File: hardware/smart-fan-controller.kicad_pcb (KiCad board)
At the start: 2 copper layers, 80 x 60 mm, 20 parts, among them J1 SATA-15PIN-PWR, J2 USB-C 16P, J3 FAN1, J4 FAN2, J5 FAN3, J6 FAN4, J7 DS18B20-1, J8 DS18B20-2, SW1 RST, SW2 BOOT, SW3 WIFI CFG, U1 AMS1117-3.3 SOT-223, U2 ESP32-S3-WROOM-1-N16R8, U3 74AHCT125 SOIC-14, U4 BME280 LGA-8

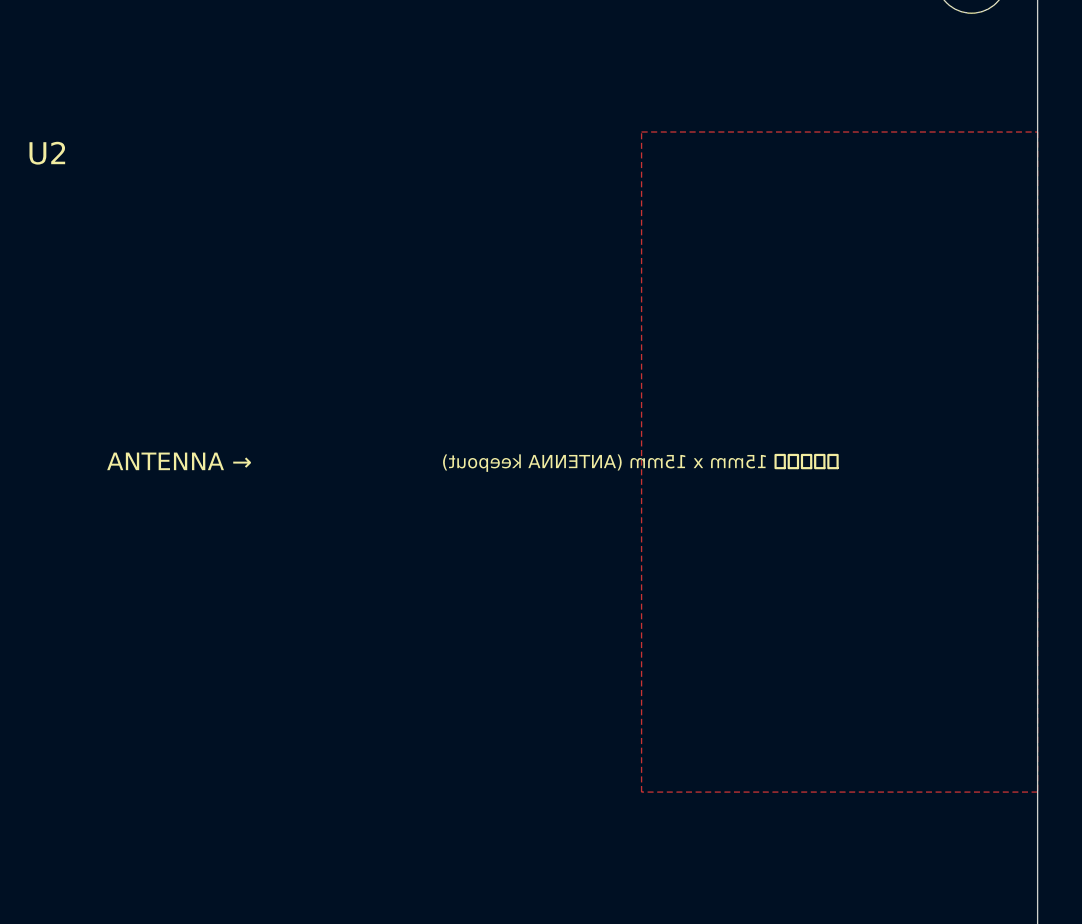
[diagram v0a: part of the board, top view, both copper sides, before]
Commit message: fix: remove v7 keepout zone for KiCad v10 compatibility
- KiCad v7 format (version 20221018) incompatible with v10
- Remove zone definition to allow file to open in v10
- Keepout area marked with silkscreen text for manual re-creation
- v10 will auto-upgrade file format on first save
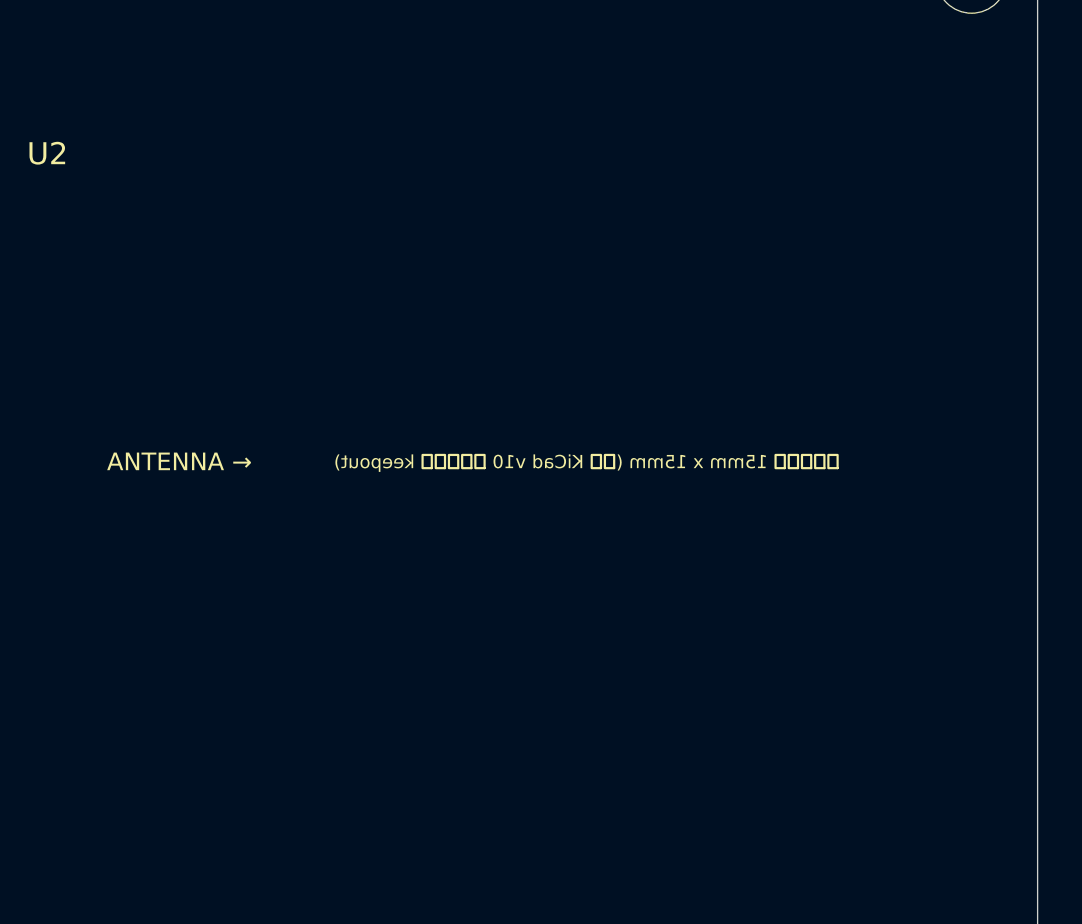
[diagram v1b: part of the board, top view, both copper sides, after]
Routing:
- removed copper zone on F.Cu, net 0
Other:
- board text added: "天线禁布区 15mm x 15mm (需在 KiCad v10 中手动添加 keepout)"
- board text removed: "天线禁布区 15mm x 15mm (ANTENNA keepout)"
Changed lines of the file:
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@@
     )
   )
-  (zone
-    (net 0) (net_name "")
-    (layer "F.Cu")
-    (name "ANTENNA_KEEPOUT_15mm")
-    (hatch edge 0.5)
-    (connect_pads (clearance 0))
-    (min_thickness 0.25)
-    (keepout_constraints
-      (kcq_tracks no) (kcq_vias no) (kcq_copperpour no)
-      (kcq_footprints no) (kcq_text no)
-    )
-    (polygon
-      (pts
-        (xy 62 10) (xy 80 10) (xy 80 40) (xy 62 40)
-      )
-    )
-  )
-  (gr_text "天线禁布区 15mm x 15mm (ANTENNA keepout)" (at 71 25 0)
+  (gr_text "天线禁布区 15mm x 15mm (需在 KiCad v10 中手动添加 keepout)" (at 71 25 0)
     (layer "F.SilkS")
     (effects (font (size 0.6 0.6) (thickness 0.1)) (justify left mirror))
